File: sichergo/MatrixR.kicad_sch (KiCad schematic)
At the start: 36 parts, among them SW17 SW_Push, SW18 SW_Push, SW22 SW_Push, SW23 SW_Push, SW24 SW_Push, SW25 SW_Push, SW26 SW_Push, SW27 SW_Push, SW28 SW_Push, SW29 SW_Push, SW30 SW_Push, SW31 SW_Push, SW32 SW_Push, SW33 SW_Push, SW34 SW_Push, SW35 SW_Push, SW36 SW_Push, SW37 SW_Push

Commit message: Added footprints to switches
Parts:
- SW17, SW18, SW22, SW23, SW24, SW25, SW26, SW27, SW28, SW29, SW30, SW31, SW32, SW33, SW34, SW35, SW36, SW37: footprint (none) -> personal:Gateron_Milky_Yellow
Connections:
- net KB_COL_0: now reaches SW17.1, SW18.1, SW22.1, SW29.1
- net KB_COL_6: now reaches D22.1 (K), D25.1 (K), D28.1 (K), D32.1 (K), D36.1 (K)
- net KB_COL_3: now reaches SW30.1, SW31.1, SW32.1
- net KB_COL_4: now reaches SW34.1, SW35.1, SW36.1
- net KB_COL_5: now reaches D18.1 (K), D24.1 (K), D27.1 (K), D31.1 (K), D35.1 (K)
- net KB_COL_2: now reaches SW26.1, SW27.1, SW28.1, SW37.1
- net KB_COL_1: now reaches SW23.1, SW24.1, SW25.1, SW33.1
- net KB_COL_7: now reaches D29.1 (K), D33.1 (K), D37.1 (K)
- net KB_ROW_4: now reaches D17.1 (K), D23.1 (K), D26.1 (K), D30.1 (K), D34.1 (K)
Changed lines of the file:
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@@
+		)
+	)
+	(hierarchical_label "KB_COL_7"
+		(shape input)
+		(at 44.45 93.98 180)
+		(effects
+			(font
+				(size 1.27 1.27)
+			)
+			(justify right)
+		)
+	)
+	(hierarchical_label "KB_COL_4"
+		(shape input)
+		(at 143.51 24.13 90)
+		(effects
+			(font
+				(size 1.27 1.27)
+			)
+			(justify left)
+		)
+	)
+	(hierarchical_label "KB_ROW_4"
+		(shape input)
+		(at 38.1 40.64 180)
+		(effects
+			(font
+				(size 1.27 1.27)
+			)
+			(justify right)
+		)
+	)
+	(hierarchical_label "KB_COL_5"
+		(shape input)
+		(at 38.1 57.15 180)
+		(effects
+			(font
+				(size 1.27 1.27)
+			)
+			(justify right)
+		)
+	)
+	(hierarchical_label "KB_COL_3"
+		(shape input)
+		(at 119.38 24.13 90)
+		(effects
+			(font
+				(size 1.27 1.27)
+			)
+			(justify left)
+		)
+	)
+	(hierarchical_label "KB_COL_6"
+		(shape input)
+		(at 38.1 74.93 180)
+		(effects
+			(font
+				(size 1.27 1.27)
+			)
+			(justify right)
+		)
+	)
+	(hierarchical_label "KB_COL_1"
+		(shape input)
+		(at 72.39 24.13 90)
+		(effects
+			(font
+				(size 1.27 1.27)
+			)
+			(justify left)
+		)
+	)
+	(hierarchical_label "KB_COL_0"
+		(shape input)
+		(at 48.26 24.13 90)
+		(effects
+			(font
+				(size 1.27 1.27)
+			)
+			(justify left)
+		)
+	)
+	(hierarchical_label "KB_COL_2"
+		(shape input)
+		(at 95.25 24.13 90)
+		(effects
+			(font
+				(size 1.27 1.27)
+			)
+			(justify left)
 		)
 	)
@@
 			)
 		)
-		(property "Footprint" ""
+		(property "Footprint" "personal:Gateron_Milky_Yellow"
 			(at 53.34 60.96 0)
 			(effects
@@
 			)
 		)
-		(property "Footprint" ""
+		(property "Footprint" "personal:Gateron_Milky_Yellow"
 			(at 53.34 43.18 0)
 			(effects
@@
 			)
 		)
-		(property "Footprint" ""
+		(property "Footprint" "personal:Gateron_Milky_Yellow"
 			(at 124.46 60.96 0)
 			(effects
@@
 			)
 		)
-		(property "Footprint" ""
+		(property "Footprint" "personal:Gateron_Milky_Yellow"
 			(at 148.59 26.67 0)
 			(effects
@@
 			)
 		)
-		(property "Footprint" ""
+		(property "Footprint" "personal:Gateron_Milky_Yellow"
 			(at 100.33 60.96 0)
 			(effects
@@
 			)
 		)
-		(property "Footprint" ""
+		(property "Footprint" "personal:Gateron_Milky_Yellow"
 			(at 77.47 43.18 0)
 			(effects
@@
 			)
 		)
-		(property "Footprint" ""
+		(property "Footprint" "personal:Gateron_Milky_Yellow"
 			(at 53.34 80.01 0)
 			(effects
@@
 			)
 		)
-		(property "Footprint" ""
+		(property "Footprint" "personal:Gateron_Milky_Yellow"
 			(at 148.59 60.96 0)
 			(effects
@@
 			)
 		)
-		(property "Footprint" ""
+		(property "Footprint" "personal:Gateron_Milky_Yellow"
 			(at 148.59 43.18 0)
 			(effects
@@
 			)
 		)
-		(property "Footprint" ""
+		(property "Footprint" "personal:Gateron_Milky_Yellow"
 			(at 124.46 43.18 0)
 			(effects
@@
 			)
 		)
-		(property "Footprint" ""
+		(property "Footprint" "personal:Gateron_Milky_Yellow"
 			(at 100.33 80.01 0)
 			(effects
@@
 			)
 		)
-		(property "Footprint" ""
+		(property "Footprint" "personal:Gateron_Milky_Yellow"
 			(at 124.46 26.67 0)
 			(effects
@@
 			)
 		)
-		(property "Footprint" ""
+		(property "Footprint" "personal:Gateron_Milky_Yellow"
 			(at 53.34 26.67 0)
 			(effects
@@
 			)
 		)
-		(property "Footprint" ""
+		(property "Footprint" "personal:Gateron_Milky_Yellow"
 			(at 100.33 43.18 0)
 			(effects
@@
 			)
 		)
-		(property "Footprint" ""
+		(property "Footprint" "personal:Gateron_Milky_Yellow"
 			(at 100.33 26.67 0)
 			(effects
@@
 			)
 		)
-		(property "Footprint" ""
+		(property "Footprint" "personal:Gateron_Milky_Yellow"
 			(at 77.47 60.96 0)
 			(effects
@@
 			)
 		)
-		(property "Footprint" ""
+		(property "Footprint" "personal:Gateron_Milky_Yellow"
 			(at 77.47 80.01 0)
 			(effects
@@
 			)
 		)
-		(property "Footprint" ""
+		(property "Footprint" "personal:Gateron_Milky_Yellow"
 			(at 77.47 26.67 0)
 			(effects

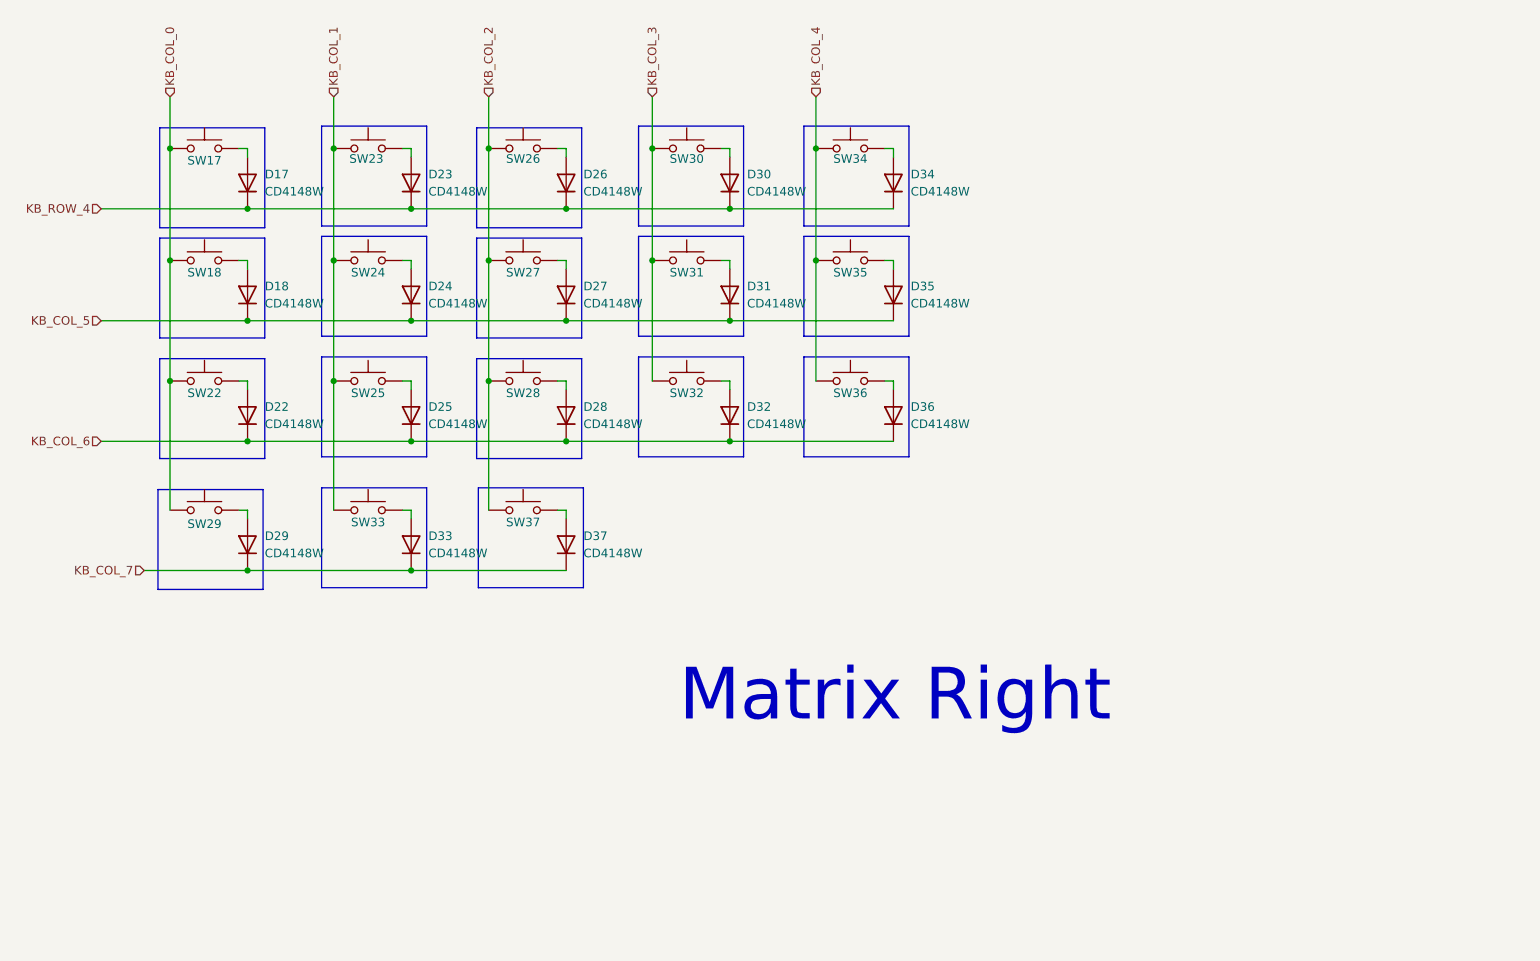
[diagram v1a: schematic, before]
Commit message: Add backlight and switch connections
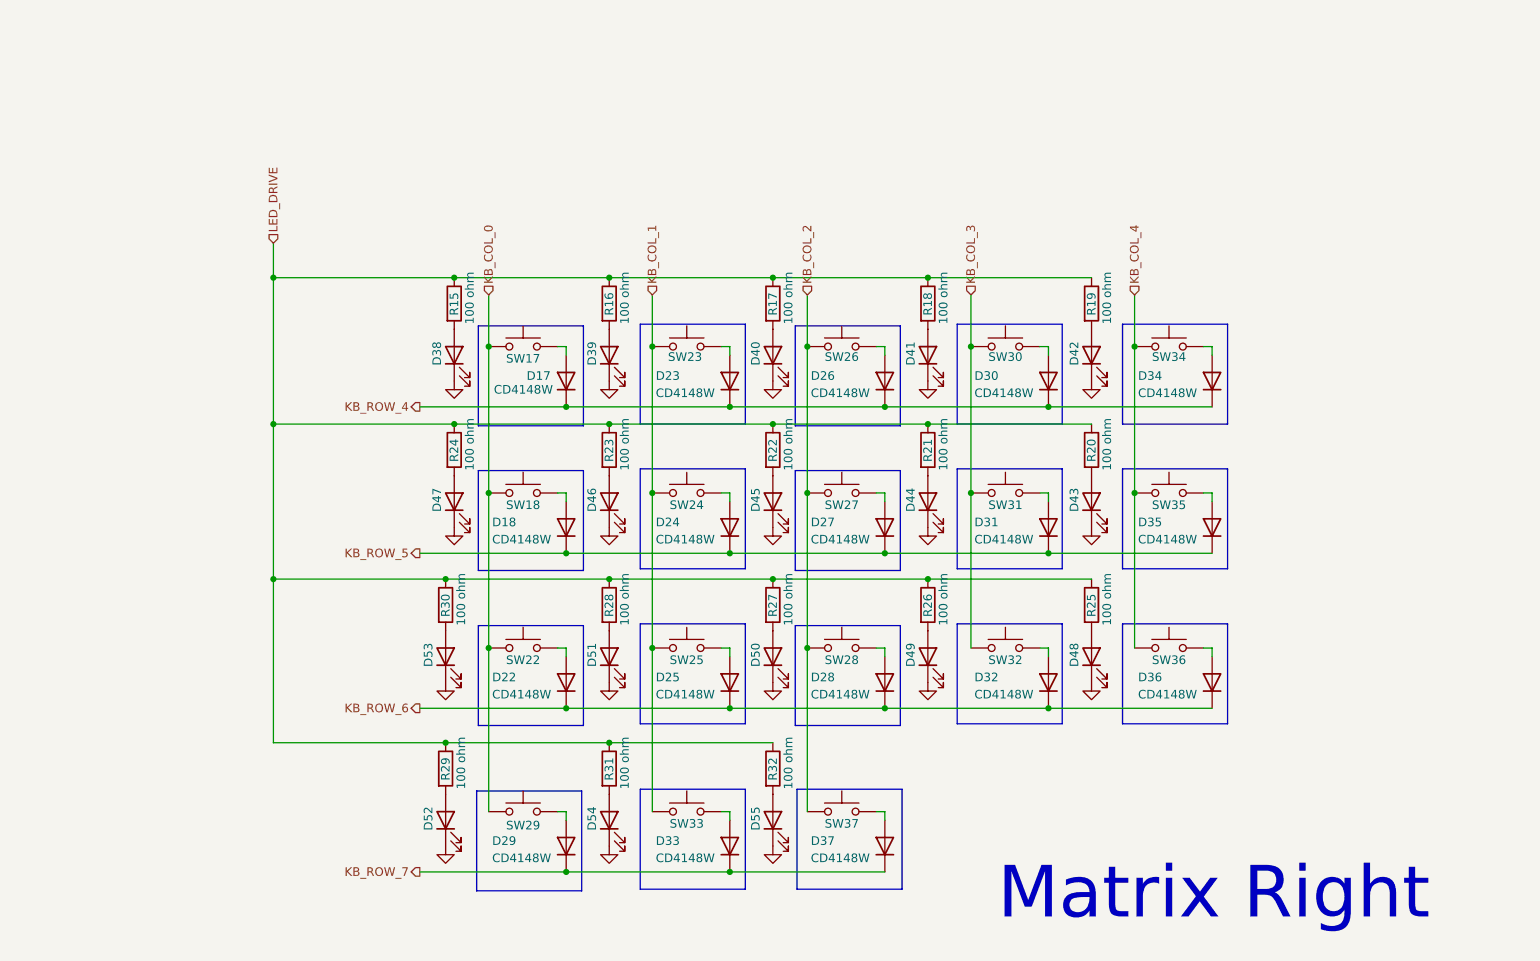
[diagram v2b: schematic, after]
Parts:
- added D38, D39, D40, D41, D42, D43, D44, D45, D46, D47, D48, D49, D50, D51, D52, D53, D54, D55: LED, LED_SMD:LED_0603_1608Metric_Pad1.05x0.95mm_HandSolder, symbol Device:LED
- added R15, R16, R17, R18, R19, R20, R21, R22, R23, R24, R25, R26, R27, R28, R29, R30, R31, R32: 100 ohm, Resistor_SMD:R_0805_2012Metric_Pad1.20x1.40mm_HandSolder, symbol #inventree:ERJ-6GEYJ101V
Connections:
- net KB_COL_5 renamed KB_ROW_5
- net KB_COL_6 renamed KB_ROW_6
- net KB_COL_7 renamed KB_ROW_7
- new net: D40.2 (A), R17.2
- new net: D38.2 (A), R15.2
- new net: D41.2 (A), R18.2
- new net: D55.2 (A), R32.2
- new net: D46.2 (A), R23.2
- new net: D44.2 (A), R21.2
- new net: D53.2 (A), R30.2
- new net: D45.2 (A), R22.2
- new net: D52.2 (A), R29.2
- new net: D49.2 (A), R26.2
- new net: D50.2 (A), R27.2
- new net: D48.2 (A), R25.2
- new net: D39.2 (A), R16.2
- new net: D42.2 (A), R19.2
- new net: D43.2 (A), R20.2
- new net: D47.2 (A), R24.2
- new net: D54.2 (A), R31.2
- new net: D51.2 (A), R28.2
- new net GND: D38.1 (K), D39.1 (K), D40.1 (K), D41.1 (K), D42.1 (K), D43.1 (K), D44.1 (K), D45.1 (K), D46.1 (K), D47.1 (K), D48.1 (K), D49.1 (K), D50.1 (K), D51.1 (K), D52.1 (K), D53.1 (K), D54.1 (K), D55.1 (K)
- new net LED_DRIVE: R15.1, R16.1, R17.1, R18.1, R19.1, R20.1, R21.1, R22.1, R23.1, R24.1, R25.1, R26.1, R27.1, R28.1, R29.1, R30.1, R31.1, R32.1
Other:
- moved on the sheet: D17, D18, D22, D23, D24, D25, D26, D27, D28, D29, D30, D31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

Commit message: Pre finish layout
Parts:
- removed R15, R16, R17, R18, R19, R20, R21, R22, R23, R24, R25, R26, R27, R28, R29, R30, R31, R32: 100 ohm, Resistor_SMD:R_0805_2012Metric_Pad1.20x1.40mm_HandSolder, symbol #inventree:ERJ-6GEYJ101V
- added R15, R16, R17, R18, R19, R20, R21, R22, R23, R24, R25, R26, R27, R28, R29, R30, R31, R32: 1 kohm, Resistor_SMD:R_0603_1608Metric_Pad0.98x0.95mm_HandSolder, symbol #inventree:RC0603FR-071KL
- D38, D39, D40, D41, D42, D43, D44, D45, D46, D47, D48, D49, D50, D51, D52, D53, D54, D55: InvenTree (none) -> 67
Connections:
- net LED_DRIVE: now also R15.1, R16.1, R17.1, R18.1, R19.1, R20.1, R21.1, R22.1, R23.1, R24.1, R25.1, R26.1, R27.1, R28.1, R29.1, R30.1, R31.1, R32.1
- net at D40.2 (A): now also R17.2
- net at D38.2 (A): now also R15.2
- net at D41.2 (A): now also R23.2
- net at D55.2 (A): now also R29.2
- net at D46.2 (A): now also R27.2
- net at D44.2 (A): now also R18.2
- net at D53.2 (A): now also R31.2
- net at D45.2 (A): now also R19.2
- net at D52.2 (A): now also R32.2
- net at D49.2 (A): now also R26.2
- net at D50.2 (A): now also R25.2
- net at D48.2 (A): now also R21.2
- net at D39.2 (A): now also R16.2
- net at D42.2 (A): now also R22.2
- net at D43.2 (A): now also R20.2
- net at D47.2 (A): now also R28.2
- net at D54.2 (A): now also R30.2
- net at D51.2 (A): now also R24.2
